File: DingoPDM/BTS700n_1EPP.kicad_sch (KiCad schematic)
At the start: 13 parts, among them U20 BTS700n-1EPP

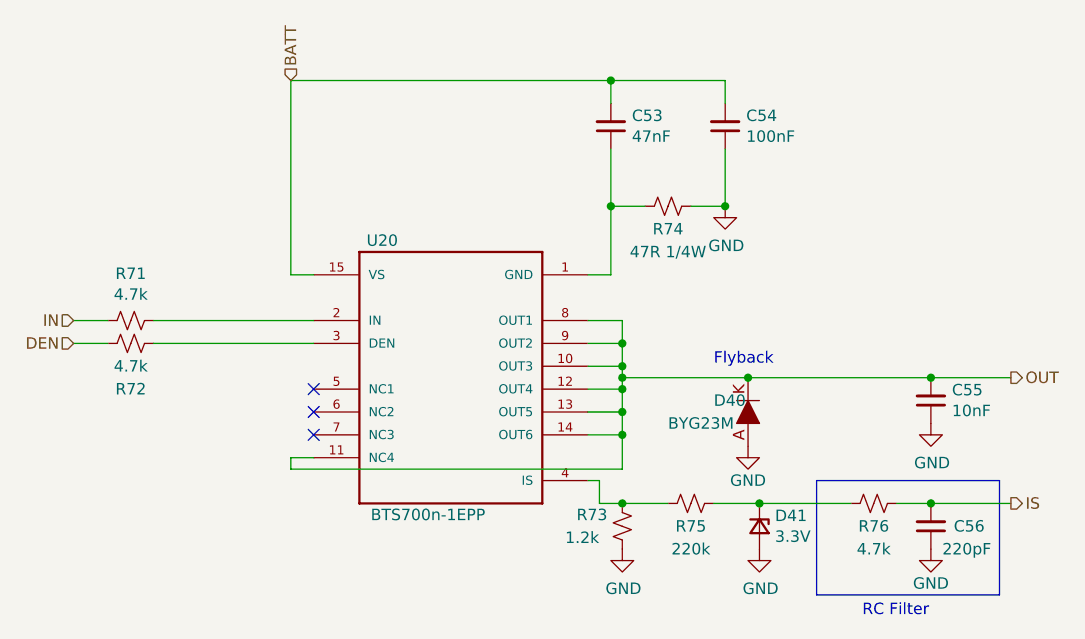
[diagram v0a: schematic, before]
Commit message: Redesigned to a smaller unit
4x high current, 2x med current, 4x low current, 2x digital inputs
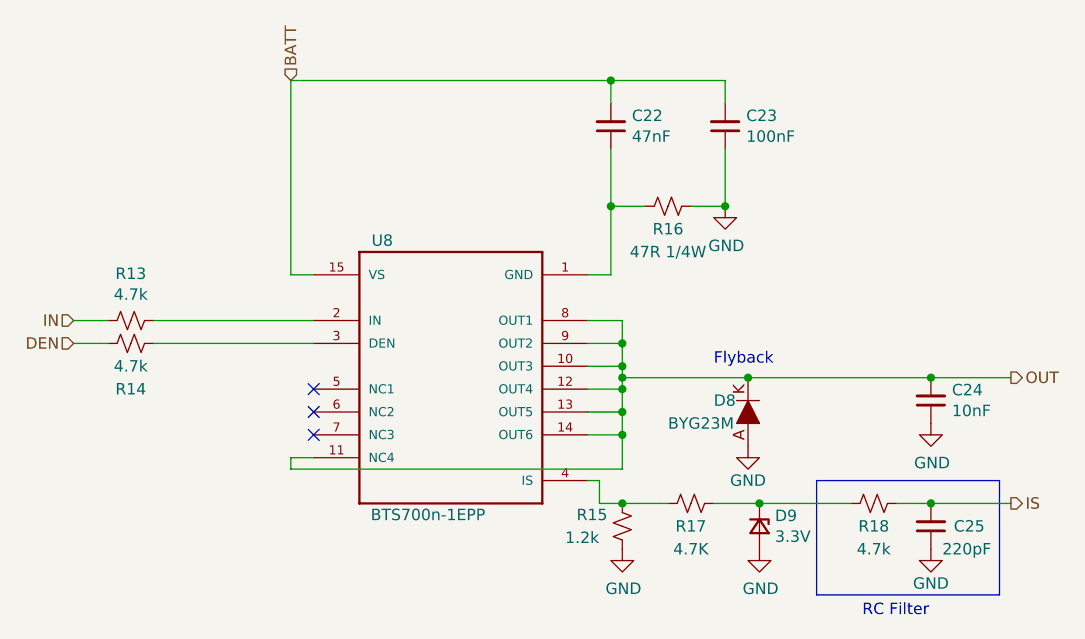
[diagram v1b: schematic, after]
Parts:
- C23: renamed from C54; LCSC (none) -> C49678
- C24: renamed from C55; LCSC (none) -> C1710
- D8: renamed from D40; LCSC (none) -> C141573
- R13: renamed from R71; LCSC (none) -> C17673
- R14: renamed from R72; LCSC (none) -> C17673
- R17: renamed from R75; value 220k -> 4.7K
- R18: renamed from R76; LCSC (none) -> C17673
- U8: renamed from U20; LCSC (none) -> C534824
- renumbered C53 to C22, C56 to C25, D41 to D9, R73 to R15, R74 to R16

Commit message: Added documentation, finished and cleaned design
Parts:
- C22: LCSC (none) -> C520039
- C25: LCSC (none) -> C576920
- D9: LCSC (none) -> C177016
- R15: LCSC (none) -> C727987
- R16: LCSC (none) -> C2907508
- R17: value 4.7K -> 4.7k; Digi-Key_PN 311-220KARCT-ND -> 311-4.70KCRCT-ND; LCSC (none) -> C17673
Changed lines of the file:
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@@
   (title_block
     (title "Dingo_PDM")
-    (date "2023-04-01")
-    (rev "v5")
+    (date "2023-07-28")
+    (rev "v6")
     (comment 3 "github.com/corygrant")
     (comment 4 "Cory Grant")
@@
       (effects (font (size 1.27 1.27)) hide)
     )
-    (property "LCSC" "" (at 149.86 68.58 0)
+    (property "LCSC" "C520039" (at 149.86 68.58 0)
       (effects (font (size 1.27 1.27)) hide)
     )
@@
       (effects (font (size 1.27 1.27)) hide)
     )
-    (property "LCSC" "" (at 156.21 77.47 0)
+    (property "LCSC" "C2907508" (at 156.21 77.47 0)
       (effects (font (size 1.27 1.27)) hide)
     )
@@
       (effects (font (size 1.27 1.27)) hide)
     )
-    (property "LCSC" "" (at 185.42 113.03 0)
+    (property "LCSC" "C576920" (at 185.42 113.03 0)
       (effects (font (size 1.27 1.27)) hide)
     )
@@
       (effects (font (size 1.27 1.27)) hide)
     )
-    (property "LCSC" "" (at 151.13 113.03 0)
+    (property "LCSC" "C727987" (at 151.13 113.03 0)
       (effects (font (size 1.27 1.27)) hide)
     )
@@
       (effects (font (size 1.27 1.27)))
     )
-    (property "Value" "4.7K" (at 158.75 115.57 90)
+    (property "Value" "4.7k" (at 158.75 115.57 90)
       (effects (font (size 1.27 1.27)))
     )
@@
       (effects (font (size 1.27 1.27)) hide)
     )
-    (property "Digi-Key_PN" "311-220KARCT-ND" (at 158.75 110.49 0)
-      (effects (font (size 1.27 1.27)) hide)
-    )
-    (property "LCSC" "" (at 158.75 110.49 0)
+    (property "Digi-Key_PN" "311-4.70KCRCT-ND" (at 158.75 110.49 0)
+      (effects (font (size 1.27 1.27)) hide)
+    )
+    (property "LCSC" "C17673" (at 158.75 110.49 0)
       (effects (font (size 1.27 1.27)) hide)
     )
@@
       (effects (font (size 1.27 1.27)) hide)
     )
-    (property "LCSC" "" (at 166.37 113.03 0)
-      (effects (font (size 1.27 1.27)) hide)
-    )
+    (property "LCSC" "C177016" (at 166.37 113.03 0)
+      (effects (font (size 1.27 1.27)) hide)
+    )

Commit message: Small edits
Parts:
- R13, R14, R17, R18: value 4.7k -> 4.7K
- R15: value 1.2k -> 1.2K
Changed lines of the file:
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@@
       (effects (font (size 1.27 1.27)))
     )
-    (property "Value" "4.7k" (at 96.52 87.2744 90)
+    (property "Value" "4.7K" (at 96.52 87.2744 90)
       (effects (font (size 1.27 1.27)))
     )
@@
       (effects (font (size 1.27 1.27)))
     )
-    (property "Value" "4.7k" (at 96.52 95.25 90)
+    (property "Value" "4.7K" (at 96.52 95.25 90)
       (effects (font (size 1.27 1.27)))
     )
@@
       (effects (font (size 1.27 1.27)))
     )
-    (property "Value" "4.7k" (at 179.07 115.57 90)
+    (property "Value" "4.7K" (at 179.07 115.57 90)
       (effects (font (size 1.27 1.27)))
     )
@@
       (effects (font (size 1.27 1.27)) (justify left))
     )
-    (property "Value" "1.2k" (at 144.78 114.3 0)
+    (property "Value" "1.2K" (at 144.78 114.3 0)
       (effects (font (size 1.27 1.27)) (justify left))
     )
@@
       (effects (font (size 1.27 1.27)))
     )
-    (property "Value" "4.7k" (at 158.75 115.57 90)
-      (effects (font (size 1.27 1.27)))
-    )
+    (property "Value" "4.7K" (at 158.75 115.57 90)
+      (effects (font (size 1.27 1.27)))
+    )

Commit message: Updated JLC zener diode part and batt volt divider
The previous zener diode had too low of a breakdown zener voltage.
The previous voltage divider was also too high of an output voltage, swapped R2 to lower the max voltage to well below the breakdown zener voltage
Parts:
- D9: LCSC C177016 -> C426855
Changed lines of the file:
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@@
       (effects (font (size 1.27 1.27)) hide)
     )
-    (property "LCSC" "C177016" (at 166.37 113.03 0)
+    (property "LCSC" "C426855" (at 166.37 113.03 0)
       (effects (font (size 1.27 1.27)) hide)
     )

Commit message: Update JLC part numbers for in stock ones
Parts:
- R15: LCSC C727987 -> C2933520
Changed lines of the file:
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@@
       (effects (font (size 1.27 1.27)) hide)
     )
-    (property "LCSC" "C727987" (at 151.13 113.03 0)
+    (property "LCSC" "C2933520" (at 151.13 113.03 0)
       (effects (font (size 1.27 1.27)) hide)
     )
